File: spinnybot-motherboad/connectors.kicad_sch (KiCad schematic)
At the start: 10 parts, among them J12 LEDSTRIP3, J13 LEDSTRIP2, J14 LEDSTRIP3, J2 LEDSTRIP1, J3 LEDSTRIP1, J4 LEDSTRIP2

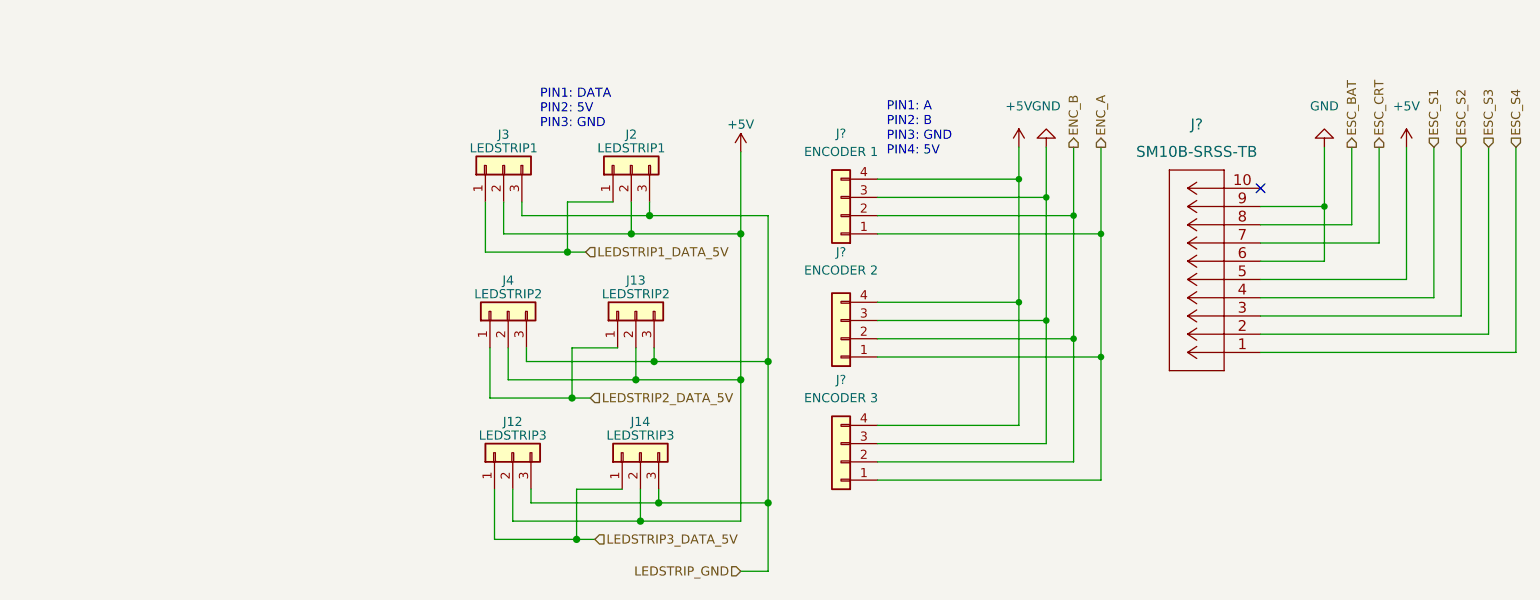
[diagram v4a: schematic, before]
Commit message: Made ESP32 connections, added logic level shifter
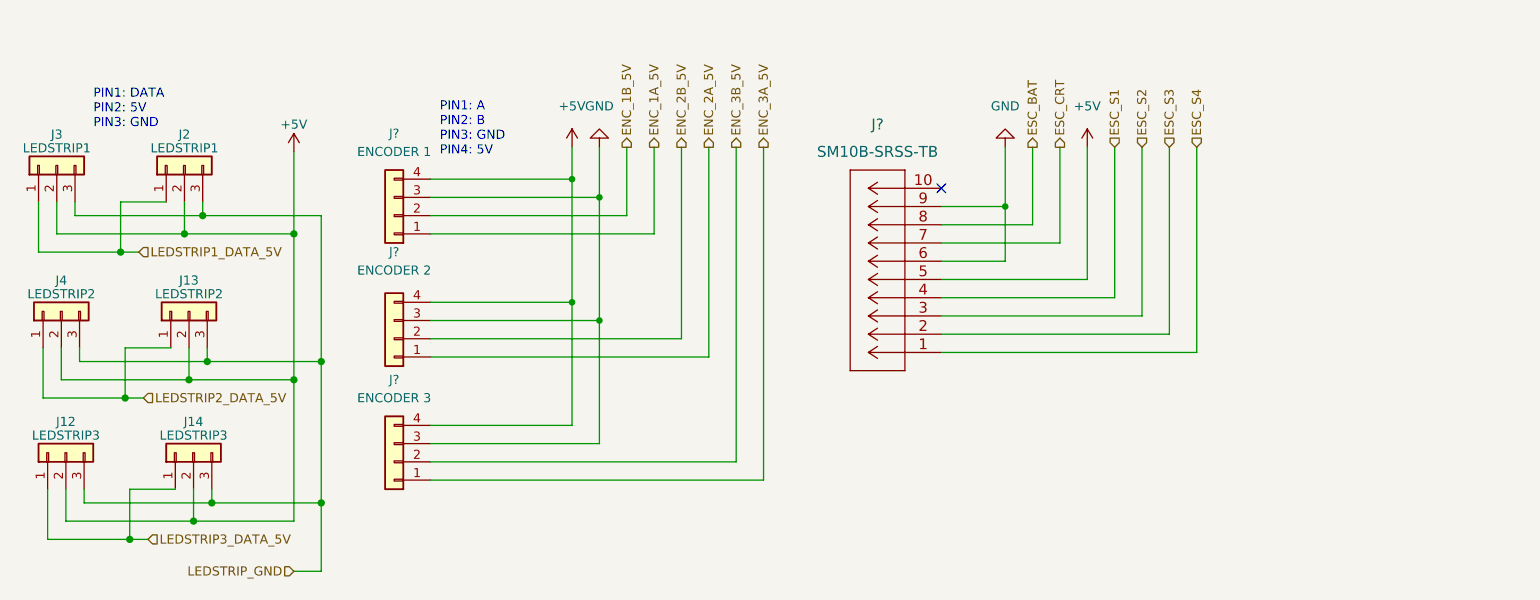
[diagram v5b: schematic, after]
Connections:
- removed net ENC_A: J?.1 (Pin_1), J?.1 (Pin_1), J?.1 (Pin_1)
- removed net ENC_B: J?.2 (Pin_2), J?.2 (Pin_2), J?.2 (Pin_2)
- new net ENC_1A_5V: J?.1 (Pin_1)
- new net ENC_1B_5V: J?.2 (Pin_2)
- new net ENC_2A_5V: J?.1 (Pin_1)
- new net ENC_2B_5V: J?.2 (Pin_2)
- new net ENC_3A_5V: J?.1 (Pin_1)
- new net ENC_3B_5V: J?.2 (Pin_2)
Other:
- moved on the sheet: J12, J13, J14, J2, J3, J4, J?

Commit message: PCB schematic (hopefully) finished
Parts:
- added JP? (x3): SolderJumper_2_Bridged, symbol Jumper:SolderJumper_2_Bridged
- added JP? (x3): SolderJumper_2_Open, symbol Jumper:SolderJumper_2_Open
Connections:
- net ESC_S1: now also JP?.2 (B), JP?.2 (B); no longer J?.4
- net ESC_S2: now also JP?.2 (B), JP?.2 (B); no longer J?.3
- net ESC_S3: now also JP?.2 (B), JP?.2 (B); no longer J?.2
- net ESC_S4: now also JP?.1 (A), JP?.1 (A), JP?.1 (A)
- new net: J?.2, JP?.1 (A)
- new net: J?.3, JP?.1 (A)
- new net: J?.4, JP?.1 (A)

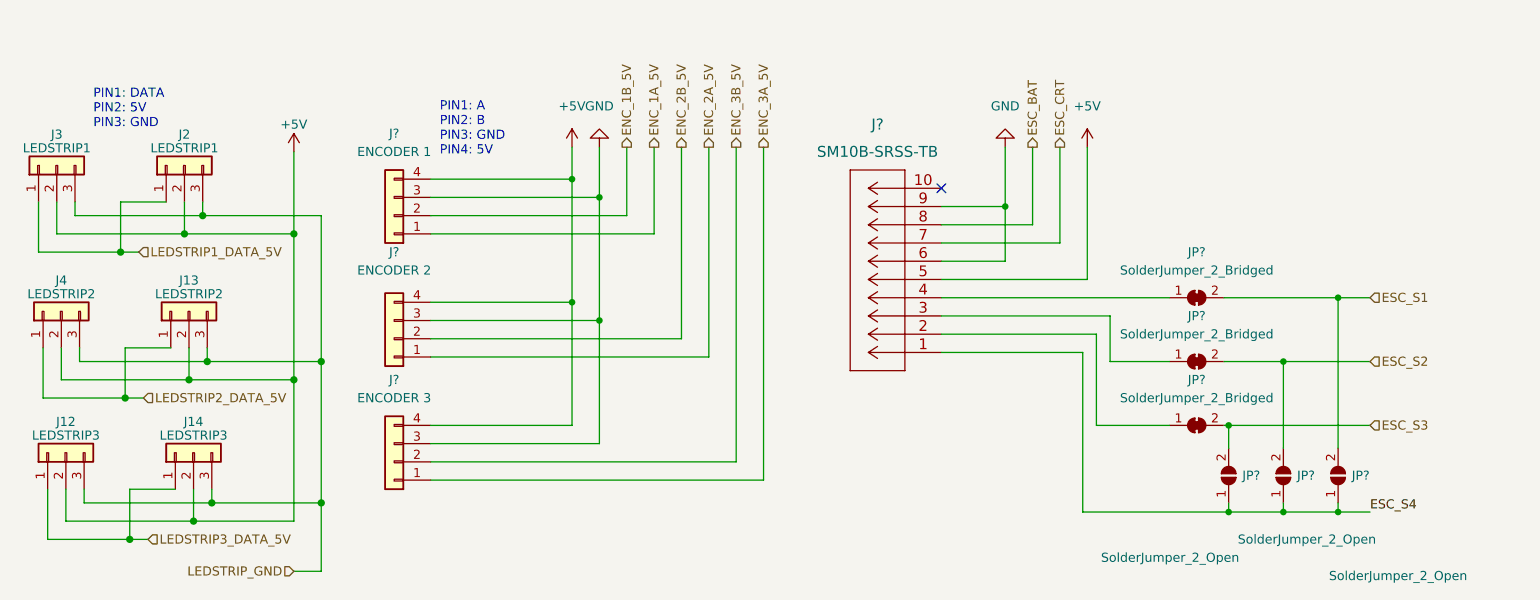
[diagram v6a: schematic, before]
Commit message: Added 4 pin JST connector footprint and assigned footprints
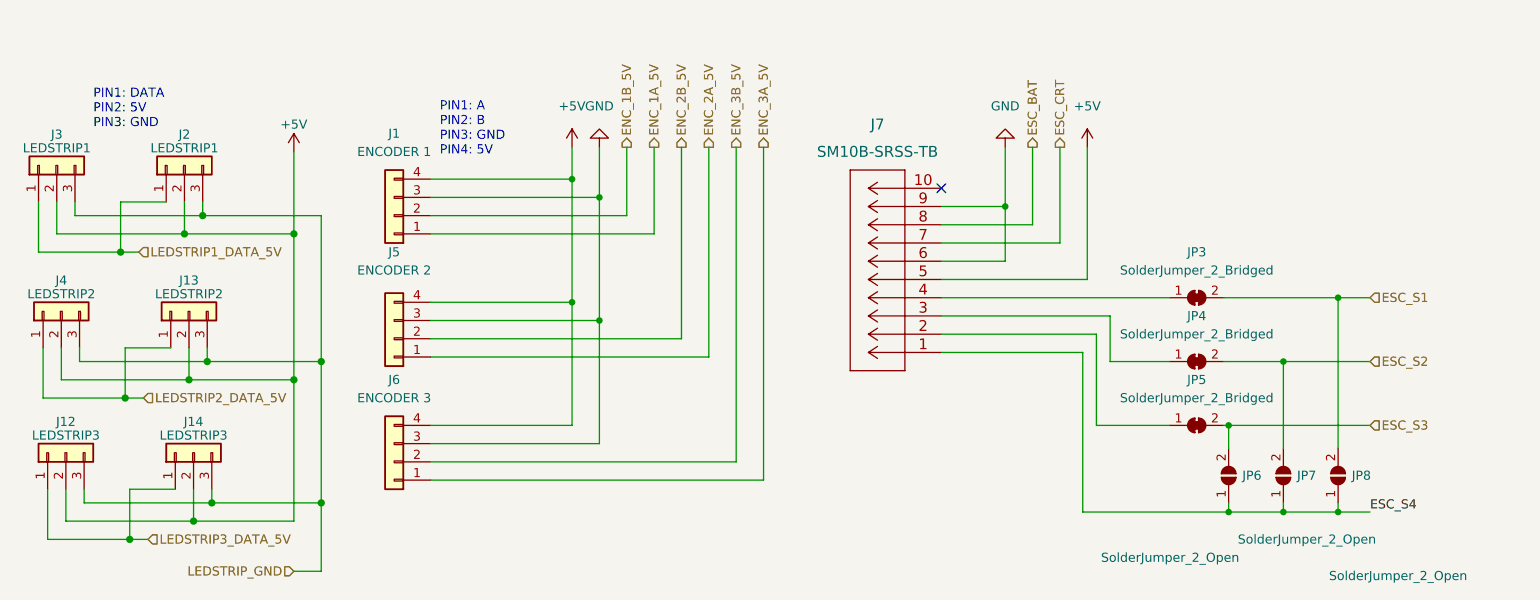
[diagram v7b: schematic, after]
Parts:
- J1, J5, J6: renamed from J?; footprint (none) -> B4B-PH-SM4-TB:B4B-PH-SM4-TBLFSN
- JP3, JP4, JP5: renamed from JP?; footprint (none) -> Jumper:SolderJumper-2_P1.3mm_Bridged_Pad1.0x1.5mm
- JP6, JP7, JP8: renamed from JP?; footprint (none) -> Jumper:SolderJumper-2_P1.3mm_Open_Pad1.0x1.5mm
- gave numbers to parts that had none: 1
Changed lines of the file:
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@@
   (symbol (lib_id "SM10B-SRSS-TB:SM10B-SRSS-TB") (at 160.02 91.44 180) (unit 1)
     (in_bom yes) (on_board yes) (fields_autoplaced)
-    (property "Reference" "J?" (id 0) (at 151.13 59.69 0)
+    (property "Reference" "J7" (id 0) (at 151.13 59.69 0)
       (effects (font (size 1.524 1.524)))
     )
@@
   (symbol (lib_id "Jumper:SolderJumper_2_Bridged") (at 195.58 83.82 0) (unit 1)
     (in_bom yes) (on_board yes) (fields_autoplaced)
-    (property "Reference" "JP?" (id 0) (at 195.58 77.47 0))
+    (property "Reference" "JP3" (id 0) (at 195.58 77.47 0))
     (property "Value" "SolderJumper_2_Bridged" (id 1) (at 195.58 80.01 0))
-    (property "Footprint" "" (id 2) (at 195.58 83.82 0)
+    (property "Footprint" "Jumper:SolderJumper-2_P1.3mm_Bridged_Pad1.0x1.5mm" (id 2) (at 195.58 83.82 0)
       (effects (font (size 1.27 1.27)) hide)
     )
@@
   (symbol (lib_id "Connector_Generic:Conn_01x04") (at 83.82 72.39 180) (unit 1)
     (in_bom yes) (on_board yes) (fields_autoplaced)
-    (property "Reference" "J?" (id 0) (at 83.82 60.96 0))
+    (property "Reference" "J1" (id 0) (at 83.82 60.96 0))
     (property "Value" "ENCODER 1" (id 1) (at 83.82 63.5 0))
-    (property "Footprint" "" (id 2) (at 83.82 72.39 0)
+    (property "Footprint" "B4B-PH-SM4-TB:B4B-PH-SM4-TBLFSN" (id 2) (at 83.82 72.39 0)
       (effects (font (size 1.27 1.27)) hide)
     )
@@
   (symbol (lib_id "Jumper:SolderJumper_2_Bridged") (at 195.58 101.6 0) (unit 1)
     (in_bom yes) (on_board yes) (fields_autoplaced)
-    (property "Reference" "JP?" (id 0) (at 195.58 95.25 0))
+    (property "Reference" "JP5" (id 0) (at 195.58 95.25 0))
     (property "Value" "SolderJumper_2_Bridged" (id 1) (at 195.58 97.79 0))
-    (property "Footprint" "" (id 2) (at 195.58 101.6 0)
+    (property "Footprint" "Jumper:SolderJumper-2_P1.3mm_Bridged_Pad1.0x1.5mm" (id 2) (at 195.58 101.6 0)
       (effects (font (size 1.27 1.27)) hide)
     )
@@
   (symbol (lib_id "Connector_Generic:Conn_01x04") (at 83.82 106.68 180) (unit 1)
     (in_bom yes) (on_board yes) (fields_autoplaced)
-    (property "Reference" "J?" (id 0) (at 83.82 95.25 0))
+    (property "Reference" "J6" (id 0) (at 83.82 95.25 0))
     (property "Value" "ENCODER 3" (id 1) (at 83.82 97.79 0))
-    (property "Footprint" "" (id 2) (at 83.82 106.68 0)
+    (property "Footprint" "B4B-PH-SM4-TB:B4B-PH-SM4-TBLFSN" (id 2) (at 83.82 106.68 0)
       (effects (font (size 1.27 1.27)) hide)
     )
@@
   (symbol (lib_id "Jumper:SolderJumper_2_Open") (at 215.265 108.585 90) (unit 1)
     (in_bom yes) (on_board yes)
-    (property "Reference" "JP?" (id 0) (at 217.17 108.585 90)
+    (property "Reference" "JP8" (id 0) (at 217.17 108.585 90)
       (effects (font (size 1.27 1.27)) (justify right))
     )
@@
       (effects (font (size 1.27 1.27)) (justify right))
     )
-    (property "Footprint" "" (id 2) (at 215.265 108.585 0)
+    (property "Footprint" "Jumper:SolderJumper-2_P1.3mm_Open_Pad1.0x1.5mm" (id 2) (at 215.265 108.585 0)
       (effects (font (size 1.27 1.27)) hide)
     )
@@
   (symbol (lib_id "Jumper:SolderJumper_2_Open") (at 207.645 108.585 90) (unit 1)
     (in_bom yes) (on_board yes)
-    (property "Reference" "JP?" (id 0) (at 209.55 108.585 90)
+    (property "Reference" "JP7" (id 0) (at 209.55 108.585 90)
       (effects (font (size 1.27 1.27)) (justify right))
     )
@@
       (effects (font (size 1.27 1.27)) (justify right))
     )
-    (property "Footprint" "" (id 2) (at 207.645 108.585 0)
+    (property "Footprint" "Jumper:SolderJumper-2_P1.3mm_Open_Pad1.0x1.5mm" (id 2) (at 207.645 108.585 0)
       (effects (font (size 1.27 1.27)) hide)
     )
@@
   (symbol (lib_id "Connector_Generic:Conn_01x04") (at 83.82 89.535 180) (unit 1)
     (in_bom yes) (on_board yes) (fields_autoplaced)
-    (property "Reference" "J?" (id 0) (at 83.82 77.47 0))
+    (property "Reference" "J5" (id 0) (at 83.82 77.47 0))
     (property "Value" "ENCODER 2" (id 1) (at 83.82 80.01 0))
-    (property "Footprint" "" (id 2) (at 83.82 89.535 0)
+    (property "Footprint" "B4B-PH-SM4-TB:B4B-PH-SM4-TBLFSN" (id 2) (at 83.82 89.535 0)
       (effects (font (size 1.27 1.27)) hide)
     )
@@
   (symbol (lib_id "Jumper:SolderJumper_2_Bridged") (at 195.58 92.71 0) (unit 1)
     (in_bom yes) (on_board yes) (fields_autoplaced)
-    (property "Reference" "JP?" (id 0) (at 195.58 86.36 0))
+    (property "Reference" "JP4" (id 0) (at 195.58 86.36 0))
     (property "Value" "SolderJumper_2_Bridged" (id 1) (at 195.58 88.9 0))
-    (property "Footprint" "" (id 2) (at 195.58 92.71 0)
+    (property "Footprint" "Jumper:SolderJumper-2_P1.3mm_Bridged_Pad1.0x1.5mm" (id 2) (at 195.58 92.71 0)
       (effects (font (size 1.27 1.27)) hide)
     )
@@
   (symbol (lib_id "Jumper:SolderJumper_2_Open") (at 200.025 108.585 90) (unit 1)
     (in_bom yes) (on_board yes)
-    (property "Reference" "JP?" (id 0) (at 201.93 108.585 90)
+    (property "Reference" "JP6" (id 0) (at 201.93 108.585 90)
       (effects (font (size 1.27 1.27)) (justify right))
     )
@@
       (effects (font (size 1.27 1.27)) (justify right))
     )
-    (property "Footprint" "" (id 2) (at 200.025 108.585 0)
-      (effects (font (size 1.27 1.27)) hide)
-    )
+    (property "Footprint" "Jumper:SolderJumper-2_P1.3mm_Open_Pad1.0x1.5mm" (id 2) (at 200.025 108.585 0)
+      (effects (font (size 1.27 1.27)) hide)
+    )

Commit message: Started board layout
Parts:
- J1, J5, J6: footprint B4B-PH-SM4-TB:B4B-PH-SM4-TBLFSN -> S4B-PH-SM4-TB:S4B-PH-SM4-TBLFSN
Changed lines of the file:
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@@
     (property "Reference" "J1" (id 0) (at 83.82 60.96 0))
     (property "Value" "ENCODER 1" (id 1) (at 83.82 63.5 0))
-    (property "Footprint" "B4B-PH-SM4-TB:B4B-PH-SM4-TBLFSN" (id 2) (at 83.82 72.39 0)
+    (property "Footprint" "S4B-PH-SM4-TB:S4B-PH-SM4-TBLFSN" (id 2) (at 83.82 72.39 0)
       (effects (font (size 1.27 1.27)) hide)
     )
@@
     (property "Reference" "J6" (id 0) (at 83.82 95.25 0))
     (property "Value" "ENCODER 3" (id 1) (at 83.82 97.79 0))
-    (property "Footprint" "B4B-PH-SM4-TB:B4B-PH-SM4-TBLFSN" (id 2) (at 83.82 106.68 0)
+    (property "Footprint" "S4B-PH-SM4-TB:S4B-PH-SM4-TBLFSN" (id 2) (at 83.82 106.68 0)
       (effects (font (size 1.27 1.27)) hide)
     )
@@
     (property "Reference" "J5" (id 0) (at 83.82 77.47 0))
     (property "Value" "ENCODER 2" (id 1) (at 83.82 80.01 0))
-    (property "Footprint" "B4B-PH-SM4-TB:B4B-PH-SM4-TBLFSN" (id 2) (at 83.82 89.535 0)
+    (property "Footprint" "S4B-PH-SM4-TB:S4B-PH-SM4-TBLFSN" (id 2) (at 83.82 89.535 0)
       (effects (font (size 1.27 1.27)) hide)
     )
